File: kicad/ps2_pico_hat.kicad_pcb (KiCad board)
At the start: 2 copper layers, 21.6 x 52.3 mm, 17 parts, among them J1 Conn_01x20_Female_left, J3 Conn_01x20_Female_right, Q1 BSS138, Q2 BSS138, Q3 BSS138, Q4 BSS138

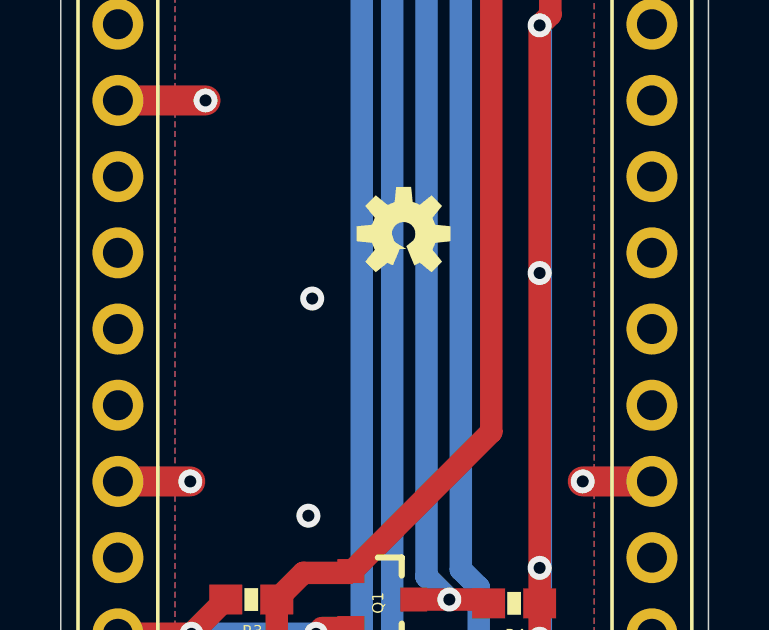
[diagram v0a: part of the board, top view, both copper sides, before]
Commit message: docs: added version number to PCB
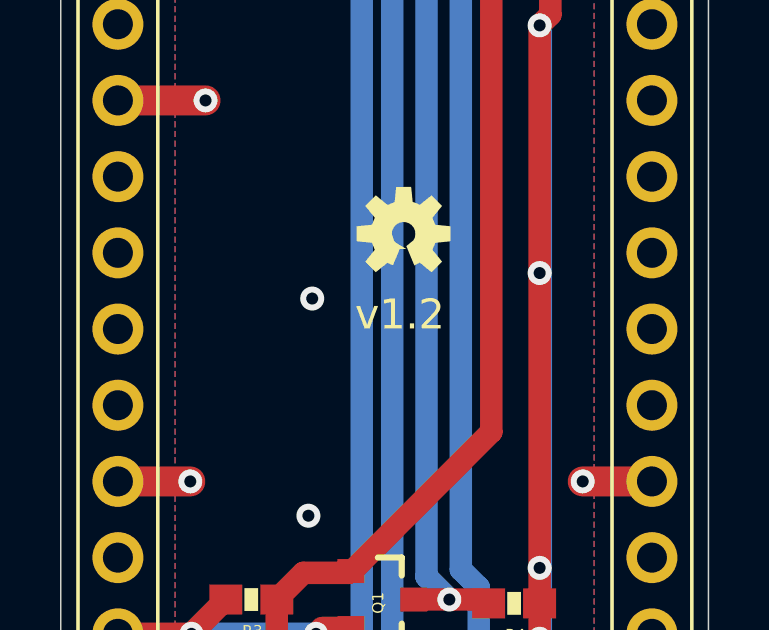
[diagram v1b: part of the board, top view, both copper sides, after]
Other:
- board text added: "v1.2"
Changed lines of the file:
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@@
   )
   (gr_rect (start 119.634 77.978) (end 98.044 130.302) (layer "Edge.Cuts") (width 0.05) (fill none))
+  (gr_text "v1.2" (at 109.4486 104.8258) (layer "B.SilkS")
+    (effects (font (size 1 1) (thickness 0.15)) (justify mirror))
+  )
+  (gr_text "v1.2" (at 109.347 104.9274) (layer "F.SilkS")
+    (effects (font (size 1 1) (thickness 0.15)))
+  )
   (segment (start 107.215 129.54) (end 107.6568 129.0982) (width 0.75) (layer "F.Cu") (net 1))
   (segment (start 104.6886 129.54) (end 107.215 129.54) (width 0.75) (layer "F.Cu") (net 1))

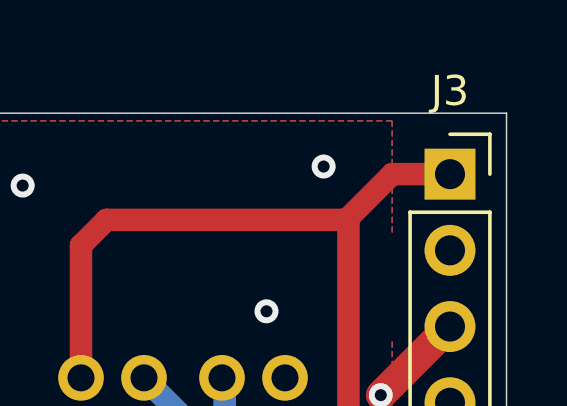
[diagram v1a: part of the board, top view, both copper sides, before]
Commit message: Improved documentation for the hat
- Changed label on J3 to J2
- Added missing links to components
- Regenerated the iBOM with links to buy components
- Removed backup files committed in error
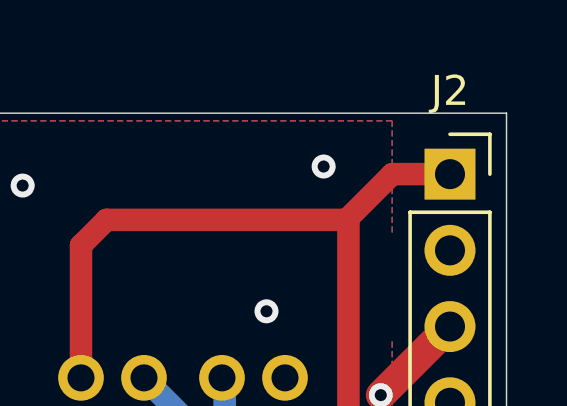
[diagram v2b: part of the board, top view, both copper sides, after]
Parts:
- renumbered J3 to J2
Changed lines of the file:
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@@
   (net 20 "unconnected-(J1-Pad5)")
   (net 21 "unconnected-(J1-Pad6)")
-  (net 22 "unconnected-(J3-Pad39)")
-  (net 23 "unconnected-(J3-Pad37)")
-  (net 24 "unconnected-(J3-Pad35)")
-  (net 25 "unconnected-(J3-Pad34)")
-  (net 26 "unconnected-(J3-Pad33)")
-  (net 27 "unconnected-(J3-Pad32)")
-  (net 28 "unconnected-(J3-Pad31)")
-  (net 29 "unconnected-(J3-Pad30)")
-  (net 30 "unconnected-(J3-Pad29)")
-  (net 31 "unconnected-(J3-Pad27)")
-  (net 32 "unconnected-(J3-Pad26)")
-  (net 33 "unconnected-(J3-Pad25)")
-  (net 34 "unconnected-(J3-Pad24)")
-  (net 35 "unconnected-(J3-Pad22)")
-  (net 36 "unconnected-(J3-Pad21)")
+  (net 22 "unconnected-(J2-Pad21)")
+  (net 23 "unconnected-(J2-Pad22)")
+  (net 24 "unconnected-(J2-Pad24)")
+  (net 25 "unconnected-(J2-Pad25)")
+  (net 26 "unconnected-(J2-Pad26)")
+  (net 27 "unconnected-(J2-Pad27)")
+  (net 28 "unconnected-(J2-Pad29)")
+  (net 29 "unconnected-(J2-Pad30)")
+  (net 30 "unconnected-(J2-Pad31)")
+  (net 31 "unconnected-(J2-Pad32)")
+  (net 32 "unconnected-(J2-Pad33)")
+  (net 33 "unconnected-(J2-Pad34)")
+  (net 34 "unconnected-(J2-Pad35)")
+  (net 35 "unconnected-(J2-Pad37)")
+  (net 36 "unconnected-(J2-Pad39)")
   (net 37 "HV")
   (net 38 "unconnected-(J1-Pad17)")
@@
     (descr "Through hole straight socket strip, 1x20, 2.54mm pitch, single row (from Kicad 4.0.7), script generated")
     (tags "Through hole socket strip THT 1x20 2.54mm single row")
+    (property "Amazon link" "https://www.amazon.com/Female-Header-Raspberry-Expansion-Breakout/dp/B0CFDV41T9/")
+    (property "Digikey link" "https://www.digikey.com/en/products/detail/adafruit-industries-llc/5585/16688065")
+    (property "Mouser link" "https://www.mouser.com/ProductDetail/Samtec/RSM-120-02-S-S-TR?qs=rU5fayqh%252BE3elhTtzhxgWw%3D%3D")
     (property "Sheetfile" "ps2_pico_hat.kicad_sch")
     (property "Sheetname" "")
     (attr through_hole)
-    (fp_text reference "J3" (at 0 -2.77) (layer "F.SilkS")
+    (fp_text reference "J2" (at 0 -2.77) (layer "F.SilkS")
       (effects (font (size 1 1) (thickness 0.15)))
     )
@@
     (fp_line (start -1.27 49.53) (end -1.27 -1.27) (layer "F.Fab") (width 0.1))
     (pad "21" thru_hole oval (at 0 48.26) (size 1.7 1.7) (drill 1) (layers *.Cu *.Mask)
-      (net 36 "unconnected-(J3-Pad21)") (pinfunction "Pin_21") (pintype "no_connect"))
+      (net 22 "unconnected-(J2-Pad21)") (pinfunction "Pin_21") (pintype "no_connect"))
     (pad "22" thru_hole oval (at 0 45.72) (size 1.7 1.7) (drill 1) (layers *.Cu *.Mask)
-      (net 35 "unconnected-(J3-Pad22)") (pinfunction "Pin_22") (pintype "no_connect"))
+      (net 23 "unconnected-(J2-Pad22)") (pinfunction "Pin_22") (pintype "no_connect"))
     (pad "23" thru_hole oval (at 0 43.18) (size 1.7 1.7) (drill 1) (layers *.Cu *.Mask)
       (net 3 "/GND") (pinfunction "GND") (pintype "passive"))
     (pad "24" thru_hole oval (at 0 40.64) (size 1.7 1.7) (drill 1) (layers *.Cu *.Mask)
-      (net 34 "unconnected-(J3-Pad24)") (pinfunction "Pin_24") (pintype "no_connect"))
+      (net 24 "unconnected-(J2-Pad24)") (pinfunction "Pin_24") (pintype "no_connect"))
     (pad "25" thru_hole oval (at 0 38.1) (size 1.7 1.7) (drill 1) (layers *.Cu *.Mask)
-      (net 33 "unconnected-(J3-Pad25)") (pinfunction "Pin_25") (pintype "no_connect"))
+      (net 25 "unconnected-(J2-Pad25)") (pinfunction "Pin_25") (pintype "no_connect"))
     (pad "26" thru_hole oval (at 0 35.56) (size 1.7 1.7) (drill 1) (layers *.Cu *.Mask)
-      (net 32 "unconnected-(J3-Pad26)") (pinfunction "Pin_26") (pintype "no_connect"))
+      (net 26 "unconnected-(J2-Pad26)") (pinfunction "Pin_26") (pintype "no_connect"))
     (pad "27" thru_hole oval (at 0 33.02) (size 1.7 1.7) (drill 1) (layers *.Cu *.Mask)
-      (net 31 "unconnected-(J3-Pad27)") (pinfunction "Pin_27") (pintype "no_connect"))
+      (net 27 "unconnected-(J2-Pad27)") (pinfunction "Pin_27") (pintype "no_connect"))
     (pad "28" thru_hole oval (at 0 30.48) (size 1.7 1.7) (drill 1) (layers *.Cu *.Mask)
       (net 3 "/GND") (pinfunction "GND") (pintype "passive"))
     (pad "29" thru_hole oval (at 0 27.94) (size 1.7 1.7) (drill 1) (layers *.Cu *.Mask)
-      (net 30 "unconnected-(J3-Pad29)") (pinfunction "Pin_29") (pintype "no_connect"))
+      (net 28 "unconnected-(J2-Pad29)") (pinfunction "Pin_29") (pintype "no_connect"))
     (pad "30" thru_hole oval (at 0 25.4) (size 1.7 1.7) (drill 1) (layers *.Cu *.Mask)
-      (net 29 "unconnected-(J3-Pad30)") (pinfunction "Pin_30") (pintype "no_connect"))
+      (net 29 "unconnected-(J2-Pad30)") (pinfunction "Pin_30") (pintype "no_connect"))
     (pad "31" thru_hole oval (at 0 22.86) (size 1.7 1.7) (drill 1) (layers *.Cu *.Mask)
-      (net 28 "unconnected-(J3-Pad31)") (pinfunction "Pin_31") (pintype "no_connect"))
+      (net 30 "unconnected-(J2-Pad31)") (pinfunction "Pin_31") (pintype "no_connect"))
     (pad "32" thru_hole oval (at 0 20.32) (size 1.7 1.7) (drill 1) (layers *.Cu *.Mask)
-      (net 27 "unconnected-(J3-Pad32)") (pinfunction "Pin_32") (pintype "no_connect"))
+      (net 31 "unconnected-(J2-Pad32)") (pinfunction "Pin_32") (pintype "no_connect"))
     (pad "33" thru_hole oval (at 0 17.78) (size 1.7 1.7) (drill 1) (layers *.Cu *.Mask)
-      (net 26 "unconnected-(J3-Pad33)") (pinfunction "Pin_33") (pintype "no_connect"))
+      (net 32 "unconnected-(J2-Pad33)") (pinfunction "Pin_33") (pintype "no_connect"))
     (pad "34" thru_hole oval (at 0 15.24) (size 1.7 1.7) (drill 1) (layers *.Cu *.Mask)
-      (net 25 "unconnected-(J3-Pad34)") (pinfunction "Pin_34") (pintype "no_connect"))
+      (net 33 "unconnected-(J2-Pad34)") (pinfunction "Pin_34") (pintype "no_connect"))
     (pad "35" thru_hole oval (at 0 12.7) (size 1.7 1.7) (drill 1) (layers *.Cu *.Mask)
-      (net 24 "unconnected-(J3-Pad35)") (pinfunction "Pin_35") (pintype "no_connect"))
+      (net 34 "unconnected-(J2-Pad35)") (pinfunction "Pin_35") (pintype "no_connect"))
     (pad "36" thru_hole oval (at 0 10.16) (size 1.7 1.7) (drill 1) (layers *.Cu *.Mask)
       (net 4 "LV") (pinfunction "LV") (pintype "power_out"))
     (pad "37" thru_hole oval (at 0 7.62) (size 1.7 1.7) (drill 1) (layers *.Cu *.Mask)
-      (net 23 "unconnected-(J3-Pad37)") (pinfunction "Pin_37") (pintype "no_connect"))
+      (net 35 "unconnected-(J2-Pad37)") (pinfunction "Pin_37") (pintype "no_connect"))
     (pad "38" thru_hole oval (at 0 5.08) (size 1.7 1.7) (drill 1) (layers *.Cu *.Mask)
       (net 3 "/GND") (pinfunction "GND") (pintype "passive"))
     (pad "39" thru_hole oval (at 0 2.54) (size 1.7 1.7) (drill 1) (layers *.Cu *.Mask)
-      (net 22 "unconnected-(J3-Pad39)") (pinfunction "Pin_39") (pintype "no_connect"))
+      (net 36 "unconnected-(J2-Pad39)") (pinfunction "Pin_39") (pintype "no_connect"))
     (pad "40" thru_hole rect (at 0 0) (size 1.7 1.7) (drill 1) (layers *.Cu *.Mask)
       (net 37 "HV") (pinfunction "Pin_40") (pintype "power_in"))
